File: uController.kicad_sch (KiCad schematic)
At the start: 1 part

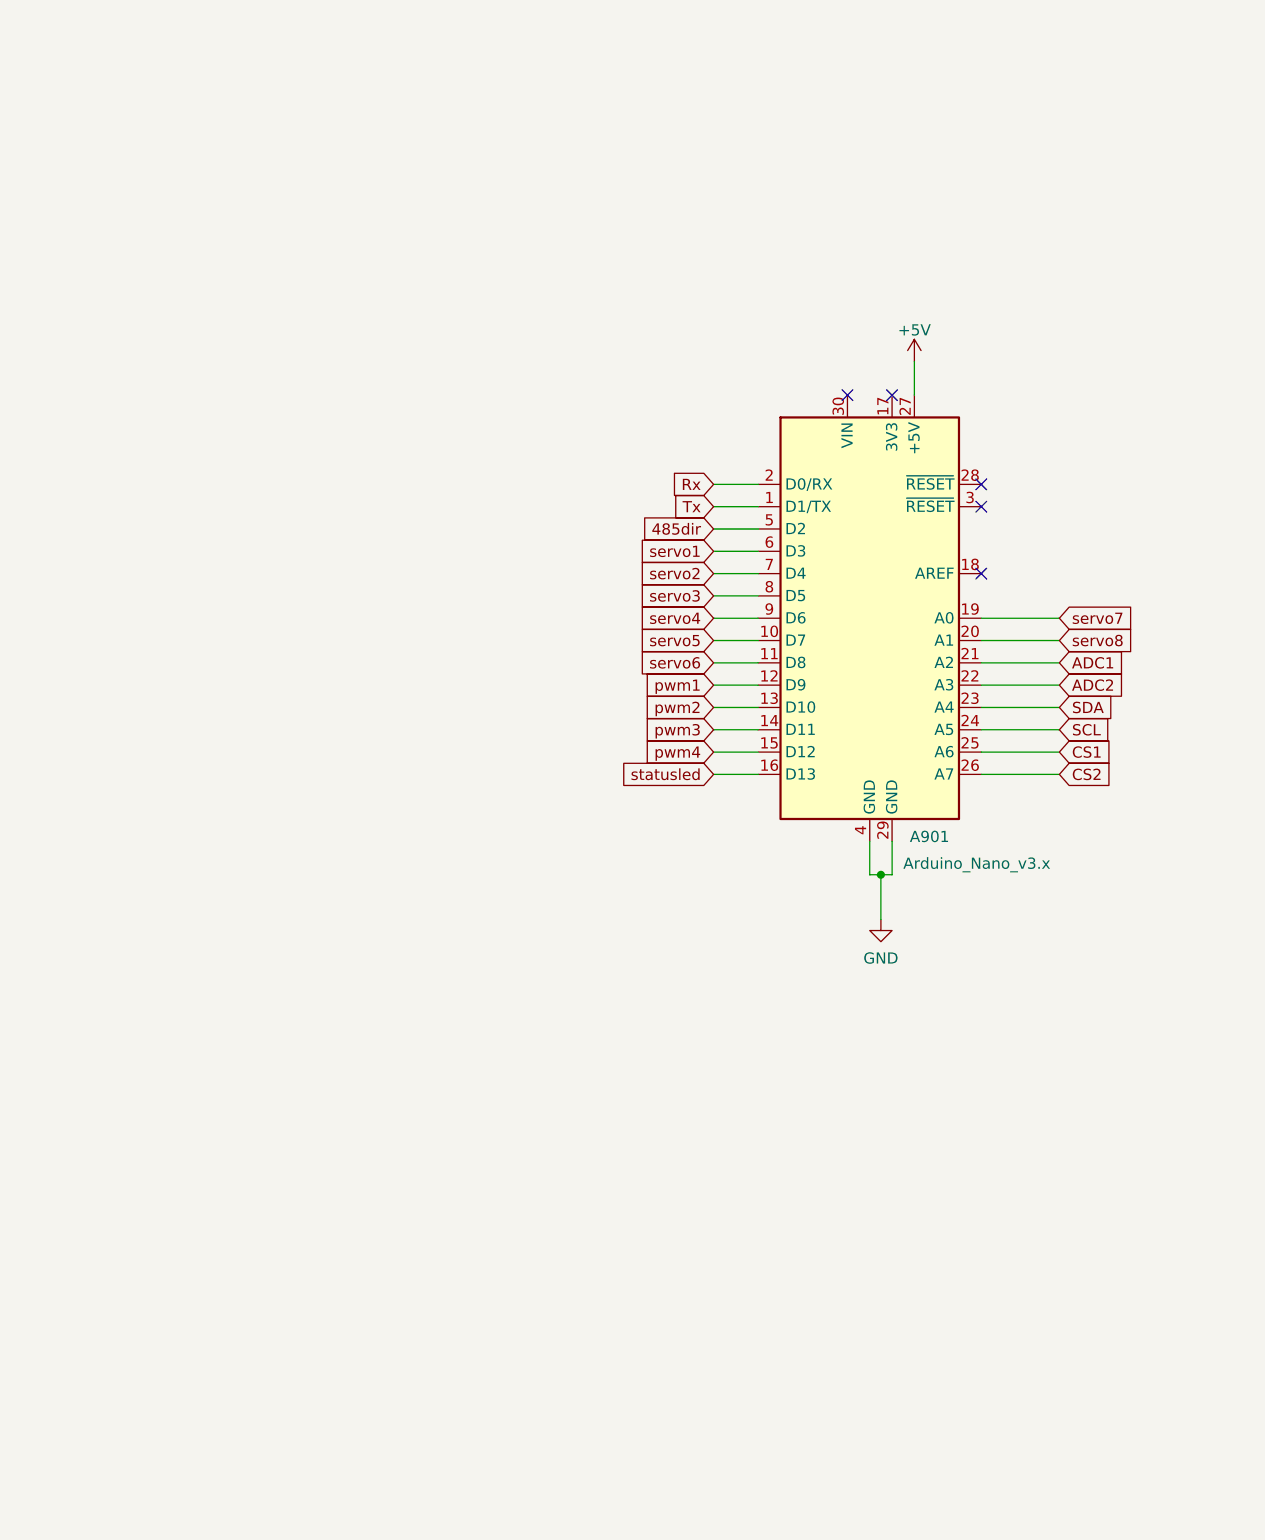
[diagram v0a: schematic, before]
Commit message: added something to debug the channel buttons
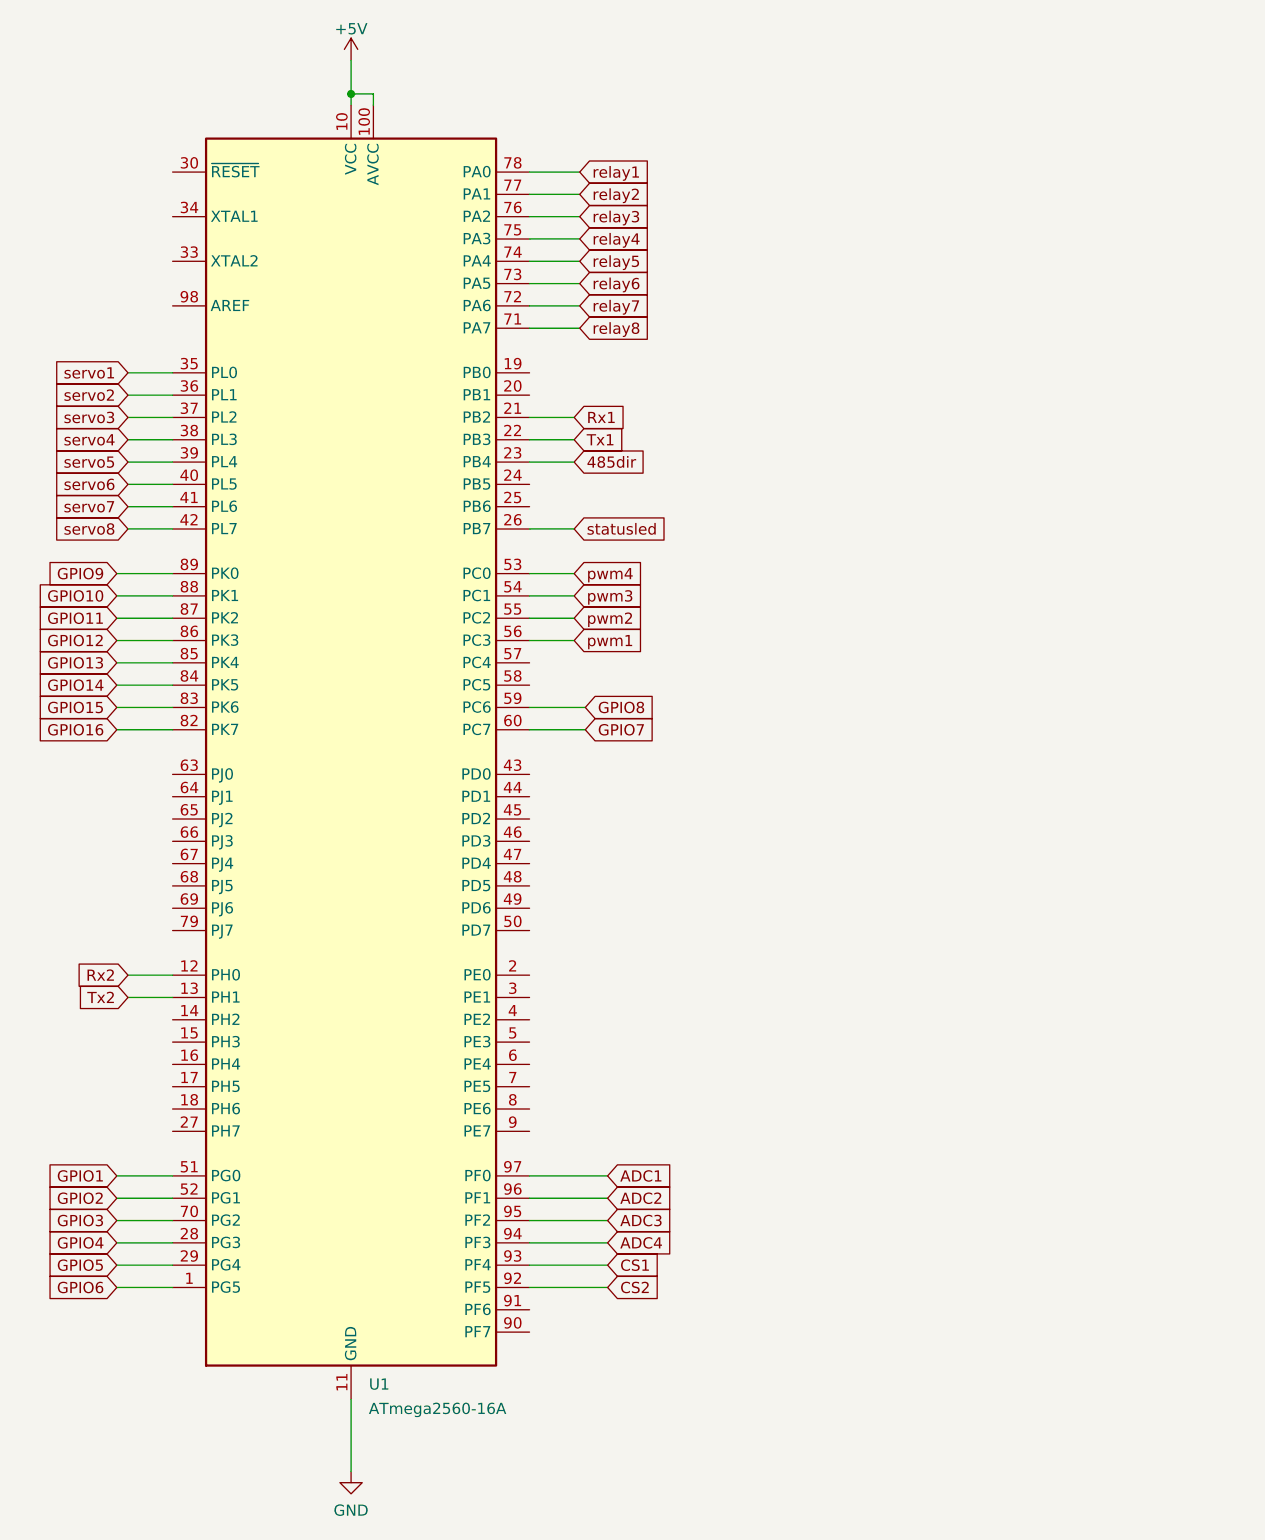
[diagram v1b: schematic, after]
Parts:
- removed A901: Arduino_Nano_v3.x, Module:Arduino_Nano, symbol MCU_Module:Arduino_Nano_v3.x
- added U1: ATmega2560-16A, Package_QFP:TQFP-100_14x14mm_P0.5mm, symbol MCU_Microchip_ATmega:ATmega2560-16A
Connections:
- net +5V: now also U1.10 (VCC), U1.100 (AVCC), U1.31 (VCC), U1.61 (VCC), U1.80 (VCC)
- net 485dir: now also U1.23 (PB4)
- net ADC1: now also U1.97 (PF0)
- net ADC2: now also U1.96 (PF1)
- net CS1: now also U1.93 (PF4)
- net CS2: now also U1.92 (PF5)
- net GND: now also U1.11 (GND), U1.32 (GND), U1.62 (GND), U1.81 (GND), U1.99 (GND)
- net pwm1: now also U1.56 (PC3)
- net pwm2: now also U1.55 (PC2)
- net pwm3: now also U1.54 (PC1)
- net pwm4: now also U1.53 (PC0)
- net servo1: now also U1.35 (PL0)
- net servo2: now also U1.36 (PL1)
- net servo3: now also U1.37 (PL2)
- net servo4: now also U1.38 (PL3)
- net servo5: now also U1.39 (PL4)
- net servo6: now also U1.40 (PL5)
- net servo7: now also U1.41 (PL6)
- net servo8: now also U1.42 (PL7)
- net statusled: now also U1.26 (PB7)
- new net ADC3: U1.95 (PF2)
- new net ADC4: U1.94 (PF3)
- new net GPIO1: U1.51 (PG0)
- new net GPIO10: U1.88 (PK1)
- new net GPIO11: U1.87 (PK2)
- new net GPIO12: U1.86 (PK3)
- new net GPIO13: U1.85 (PK4)
- new net GPIO14: U1.84 (PK5)
- new net GPIO15: U1.83 (PK6)
- new net GPIO16: U1.82 (PK7)
- new net GPIO2: U1.52 (PG1)
- new net GPIO3: U1.70 (PG2)
- new net GPIO4: U1.28 (PG3)
- new net GPIO5: U1.29 (PG4)
- new net GPIO6: U1.1 (PG5)
- new net GPIO7: U1.60 (PC7)
- new net GPIO8: U1.59 (PC6)
- new net GPIO9: U1.89 (PK0)
- new net Rx1: U1.21 (PB2)
- new net Rx2: U1.12 (PH0)
- new net Tx1: U1.22 (PB3)
- new net Tx2: U1.13 (PH1)
- new net relay1: U1.78 (PA0)
- new net relay2: U1.77 (PA1)
- new net relay3: U1.76 (PA2)
- new net relay4: U1.75 (PA3)
- new net relay5: U1.74 (PA4)
- new net relay6: U1.73 (PA5)
- new net relay7: U1.72 (PA6)
- new net relay8: U1.71 (PA7)
- no-connect marks 5 -> 0

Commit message: redid this project. I want to use an atmega328 so I ditched some IO. I retained 4 servo, 1 H-bridge (should make it double), 3 relays, 6 GPIO, 1 potentiometer and loconet interface. And I still have a config button
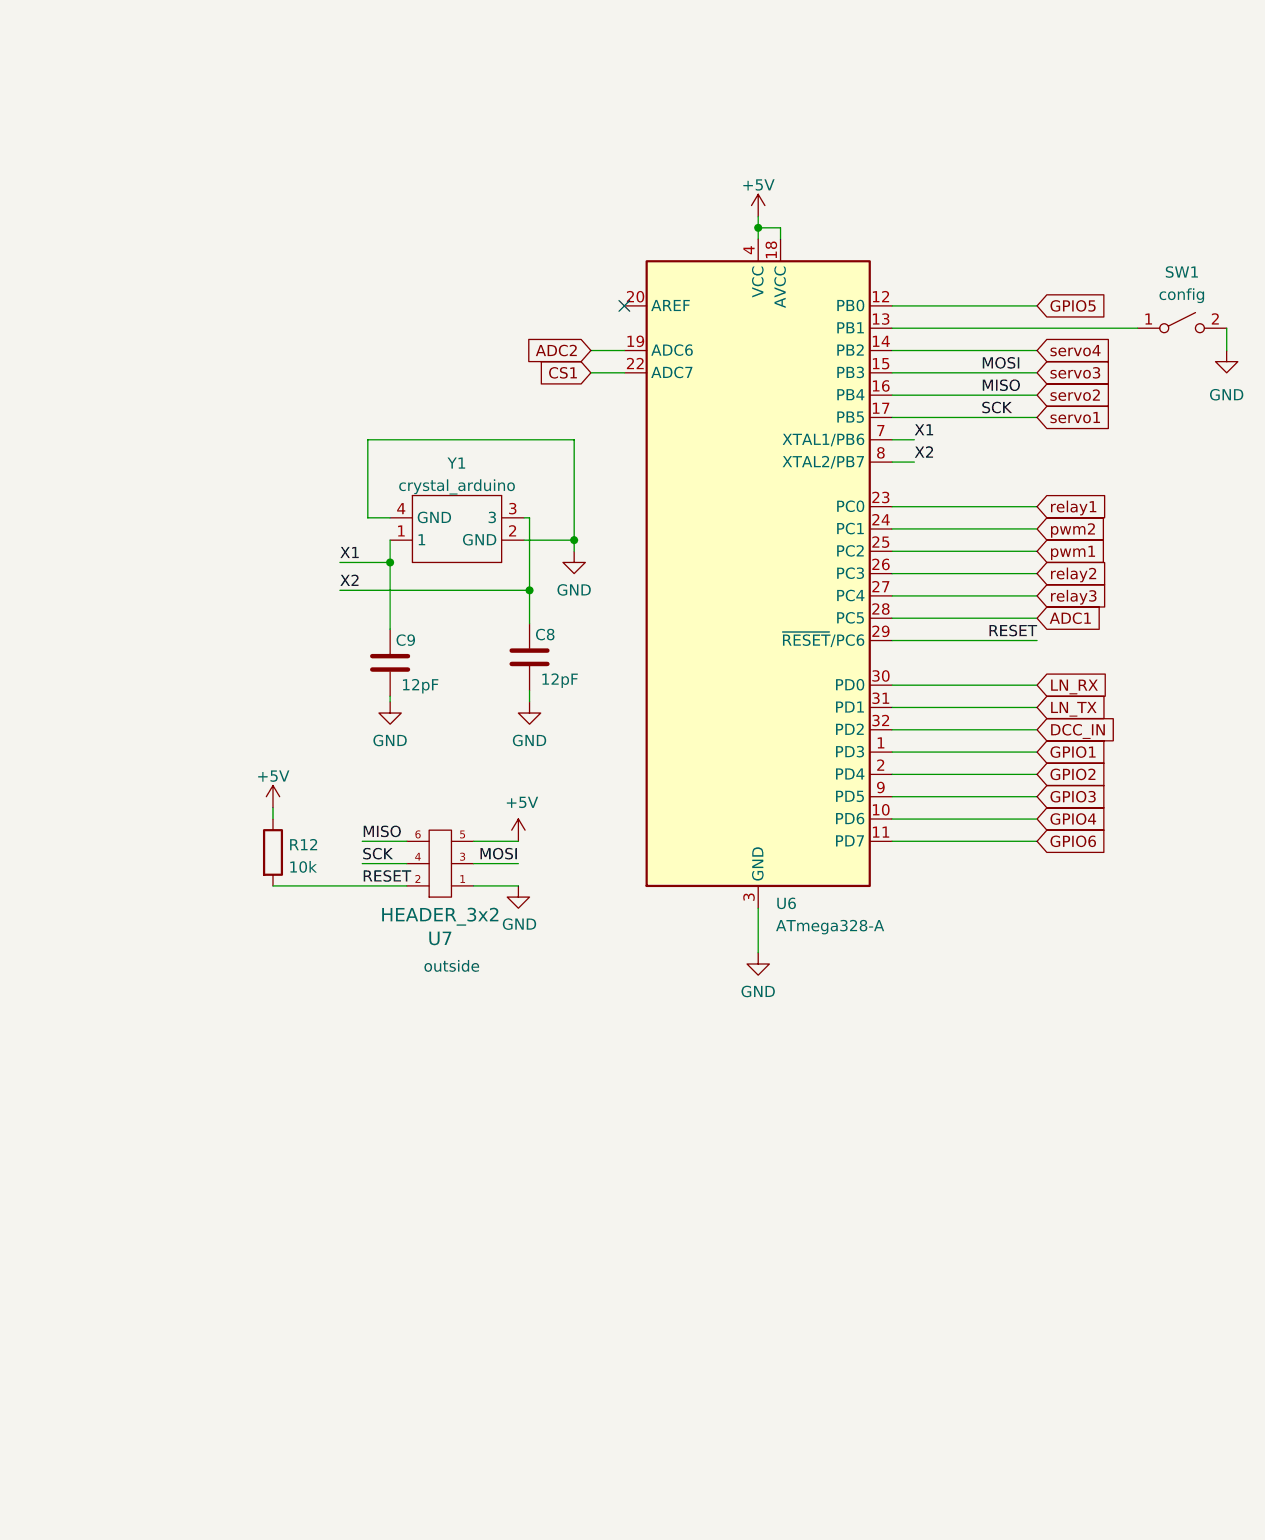
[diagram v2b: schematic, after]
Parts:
- removed U1: ATmega2560-16A, Package_QFP:TQFP-100_14x14mm_P0.5mm, symbol MCU_Microchip_ATmega:ATmega2560-16A
- added C8, C9: 12pF, Capacitor_SMD:C_0603_1608Metric_Pad1.08x0.95mm_HandSolder, symbol Device:C
- added R12: 10k, Resistor_SMD:R_0603_1608Metric_Pad0.98x0.95mm_HandSolder, symbol Device:R
- added SW1: config, Button_Switch_SMD:SW_SPST_SKQG_WithStem, symbol Switch:SW_SPST
- added U6: ATmega328-A, Package_QFP:TQFP-32_7x7mm_P0.8mm, symbol MCU_Microchip_ATmega:ATmega328-A
- added U7: HEADER_3x2, Connector_PinSocket_1.27mm:PinSocket_2x03_P1.27mm_Vertical, symbol servoDriverSMD-rescue:HEADER_3x2-w_connectors
- added Y1: crystal_arduino, custom_kicad_lib_sk:crystal_arduino, symbol custom_bas:crystal_arduino
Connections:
- net +5V: now also R12.1, U6.18 (AVCC), U6.4 (VCC), U6.6 (VCC), U7.5
- net ADC1: now also U6.28 (PC5)
- net ADC2: now also U6.19 (ADC6)
- net CS1: now also U6.22 (ADC7)
- net GND: now also C8.1, C9.1, SW1.2 (B), U6.21 (GND), U6.3 (GND), U6.5 (GND), U7.1, Y1.2 (GND), Y1.4 (GND)
- net GPIO1: now also U6.1 (PD3)
- net GPIO2: now also U6.2 (PD4)
- net GPIO3: now also U6.9 (PD5)
- net GPIO4: now also U6.10 (PD6)
- net GPIO5: now also U6.12 (PB0)
- net GPIO6: now also U6.11 (PD7)
- net pwm1: now also U6.25 (PC2)
- net pwm2: now also U6.24 (PC1)
- net relay1: now also U6.23 (PC0)
- net relay2: now also U6.26 (PC3)
- net relay3: now also U6.27 (PC4)
- net servo1: now also U6.17 (PB5), U7.4
- net servo2: now also U6.16 (PB4), U7.6
- net servo3: now also U6.15 (PB3), U7.3
- net servo4: now also U6.14 (PB2)
- new net: SW1.1 (A), U6.13 (PB1)
- new net DCC_IN: U6.32 (PD2)
- new net LN_RX: U6.30 (PD0)
- new net LN_TX: U6.31 (PD1)
- new net RESET: R12.2, U6.29 (~{RESET}/PC6), U7.2
- new net X1: C9.2, U6.7 (XTAL1/PB6), Y1.1
- new net X2: C8.2, U6.8 (XTAL2/PB7), Y1.3
- no-connect marks 0 -> 1
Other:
- note added: "outside"
